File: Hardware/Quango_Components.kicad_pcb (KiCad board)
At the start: 2 copper layers, 80.7 x 100 mm, 167 parts, among them J1 Conn_01x12_Male, J2 Conn_01x12_Male, J3 Conn_01x12_Male, J4 Conn_01x12_Male, J5 SWD_Header, J6 Eurorack_10_pin_power, Q1 MMBT3904, U1 LM1117-3.3, U10 TL074, U11 TL074, U12 TL074, U13 TL074, U14 TL074, U2 STM32G473V, U3 LM1117-5.0, U4 PS508, U5 MCP6002, U6 AS3364, U7 AS3364, U8 AD5676, U9 MCP48CMB21, Y1 8MHz 20pF

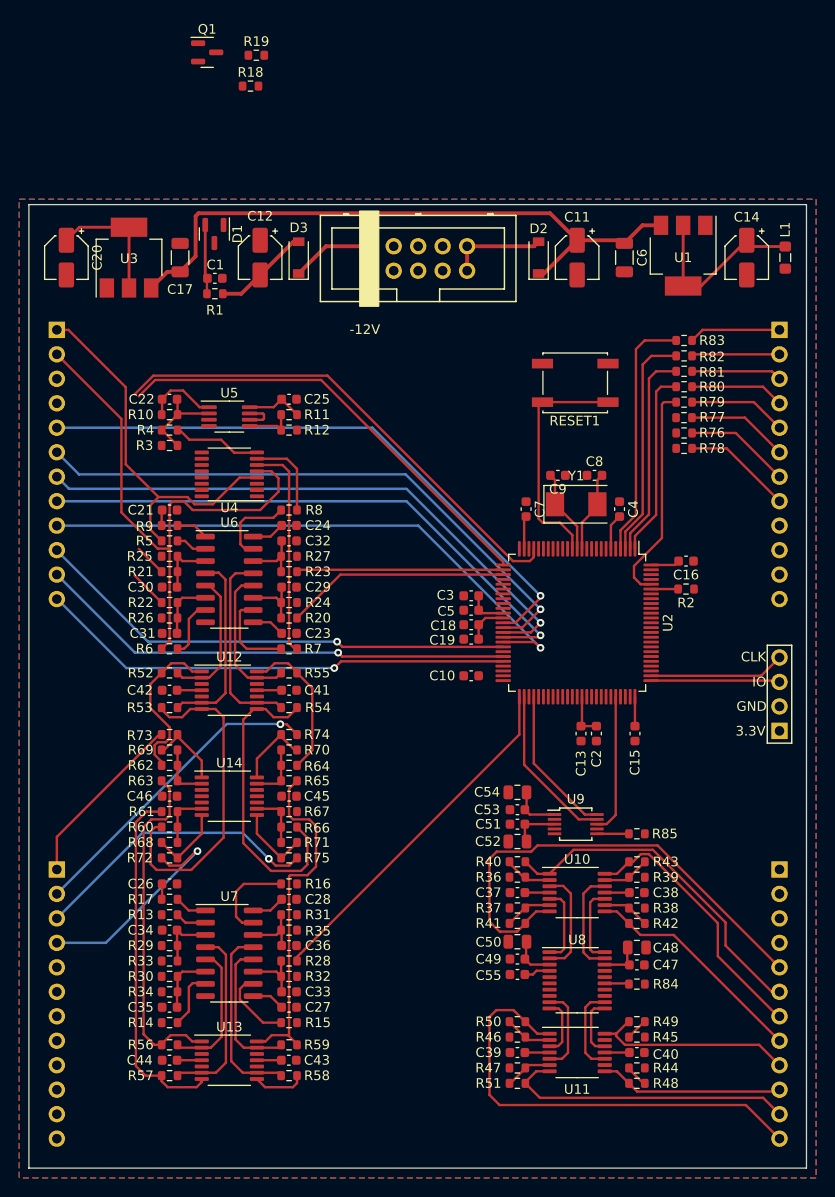
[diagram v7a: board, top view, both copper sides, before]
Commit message: First draft of signal routing done
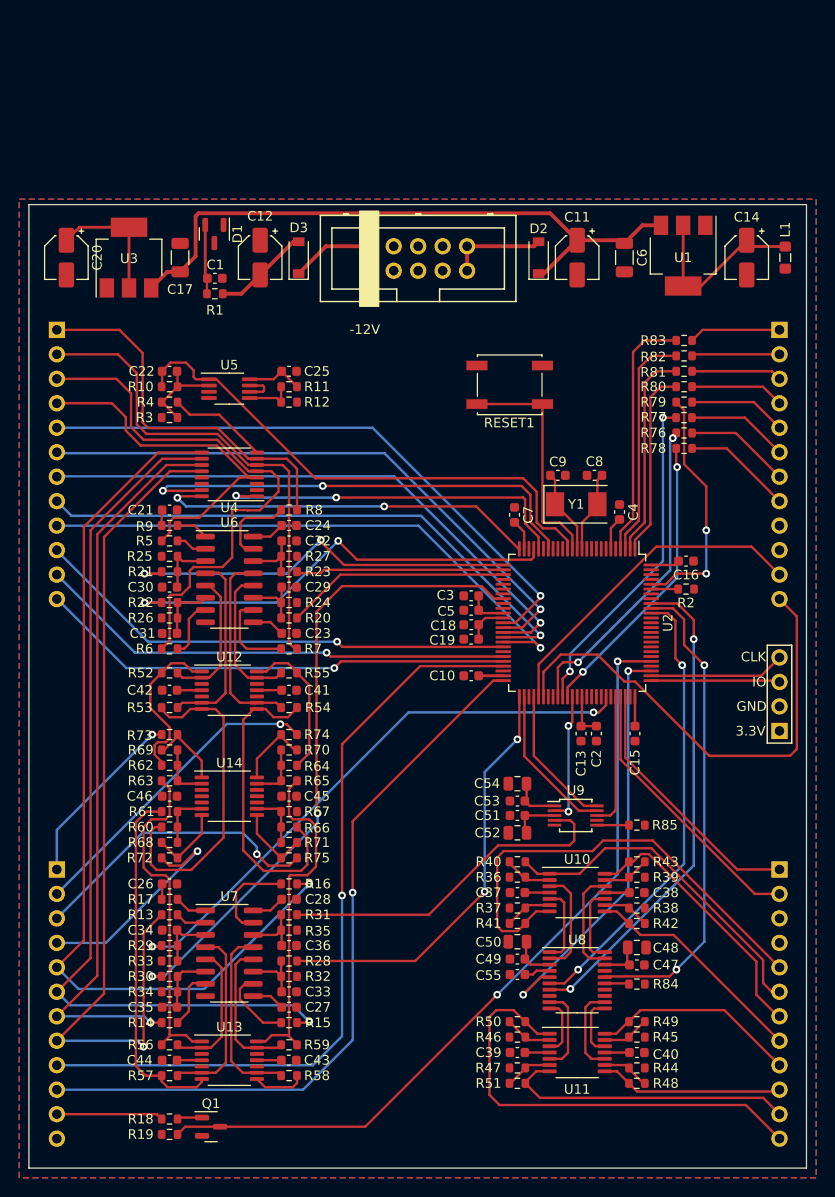
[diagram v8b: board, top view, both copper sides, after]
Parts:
- moved R19 112.4 mm to (64.7, 135.5), turned to 180 degrees
- moved Q1 111.5 mm to (69.0, 134.7)
- moved R18 107.5 mm to (64.7, 133.9)
- moved RESET1 6.80 mm to (100.0, 57.7)
- moved C22 2.90 mm to (64.7, 56.3)
- moved C25 2.90 mm to (77.1, 56.3)
- moved R10 2.90 mm to (64.7, 57.9)
- moved R11 2.90 mm to (77.1, 57.9)
- moved R12 2.90 mm to (77.1, 59.5)
- moved R3 2.90 mm to (64.7, 61.1)
- moved R4 2.90 mm to (64.7, 59.5)
- moved U5 2.90 mm to (70.9, 58.1)
- moved C7 1.34 mm to (100.5, 71.2)
- moved C54 0.90 mm to (100.8, 99.1)
- moved C51 0.90 mm to (100.8, 102.4)
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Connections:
- J1 pad 1: /AudioA1_In -> /AudioA4_In
- J1 pad 2: /AudioA2_In -> /AudioA3_In
- J1 pad 3: /AudioA3_In -> /AudioA2_In
- J1 pad 4: /AudioA4_In -> /AudioA1_In
- J2 pad 10: /USB_DM -> /Calib_Btn2
- J2 pad 5: /AudioB1_In -> /AudioB4_In
- J2 pad 6: /AudioB2_In -> /AudioB3_In
- J2 pad 7: /AudioB3_In -> /AudioB2_In
- J2 pad 8: /AudioB4_In -> /AudioB1_In
- J2 pad 9: /USB_DP -> /Calib_Btn1
- J3 pad 10: /ChannelB_Level -> GND
- J3 pad 11: +3.3VA -> /ChannelA_Level
- J3 pad 12: GND -> /ChannelB_Level
- J3 pad 9: /ChannelA_Level -> +3.3VA
- J4 pad 1: +3.3VA -> /USB_DP
- J4 pad 2: /Calib_Btn1 -> /USB_DM
- J4 pad 3: /Calib_Btn2 -> GND
- J4 pad 4: GND -> +3.3VA
- U2 pad 10: /MultiplexerA1 -> unconnected-(U2-Pad10)
- U2 pad 11: /MultiplexerA2 -> unconnected-(U2-Pad11)
- U2 pad 19: /MultiplexerA0 -> /MultiplexerA2
- U2 pad 21: unconnected-(U2-Pad21) -> /MultiplexerA0
- U2 pad 25: unconnected-(U2-Pad25) -> /MultiplexerA1
- U2 pad 47: unconnected-(U2-Pad47) -> /Calib_Btn1
- U2 pad 50: unconnected-(U2-Pad50) -> /Calib_Btn2
- U2 pad 93: /Calib_Btn2 -> unconnected-(U2-Pad93)
- U2 pad 94: /Calib_Btn1 -> unconnected-(U2-Pad94)
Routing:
- net /AudioB4_In: track 0.00 -> 95.2 mm, vias 0 -> 1
- net /AudioB3_In: track 0.00 -> 92.8 mm, vias 0 -> 1
- net /AudioB1_In: track 0.00 -> 91.0 mm, vias 0 -> 1
- net /MIDI_UART: track 0.00 -> 82.4 mm, vias 0 -> 2
- net /Calib_Btn1: track 0.00 -> 81.2 mm, vias 0 -> 1
- net /Calib_Btn2: track 0.00 -> 77.2 mm, vias 0 -> 1
- net /AudioB2_In: track 0.00 -> 76.7 mm, vias 0 -> 1
- net /EnvB2_DAC: track 0.00 -> 67.7 mm, vias 0 -> 2
- net /EnvB1_DAC: track 0.00 -> 59.4 mm, vias 0 -> 2
- net /SPI1_MOSI: track 0.00 -> 50.9 mm, vias 0 -> 2
- net /ChannelB_Level: track 0.00 -> 50.6 mm
- net /SPI1_MISO: track 0.00 -> 50.1 mm, vias 0 -> 2
- net /MultiplexerA2: track 0.00 -> 50.0 mm, vias 0 -> 2
- net /SPI1_SCK: track 0.00 -> 47.5 mm, vias 0 -> 2
- net /Audio_In_Multiplexed: track 7.55 -> 54.9 mm
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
